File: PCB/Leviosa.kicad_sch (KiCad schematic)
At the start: 76 parts, among them J1 Barrel_Jack, J2 Conn_01x05_Socket, J3 2.54mm 1x03 Spare, Q1 NCE0110K, U1 SS495A, U2 LM321, U3 TPS1H200AQDGNRQ1, U4 INA199A3DCKR, U5 LM393, U6 L78L10_SOT89, U7 MX27517, U8 AZ1117CH2-3.3, U9 STM32G030F6Px

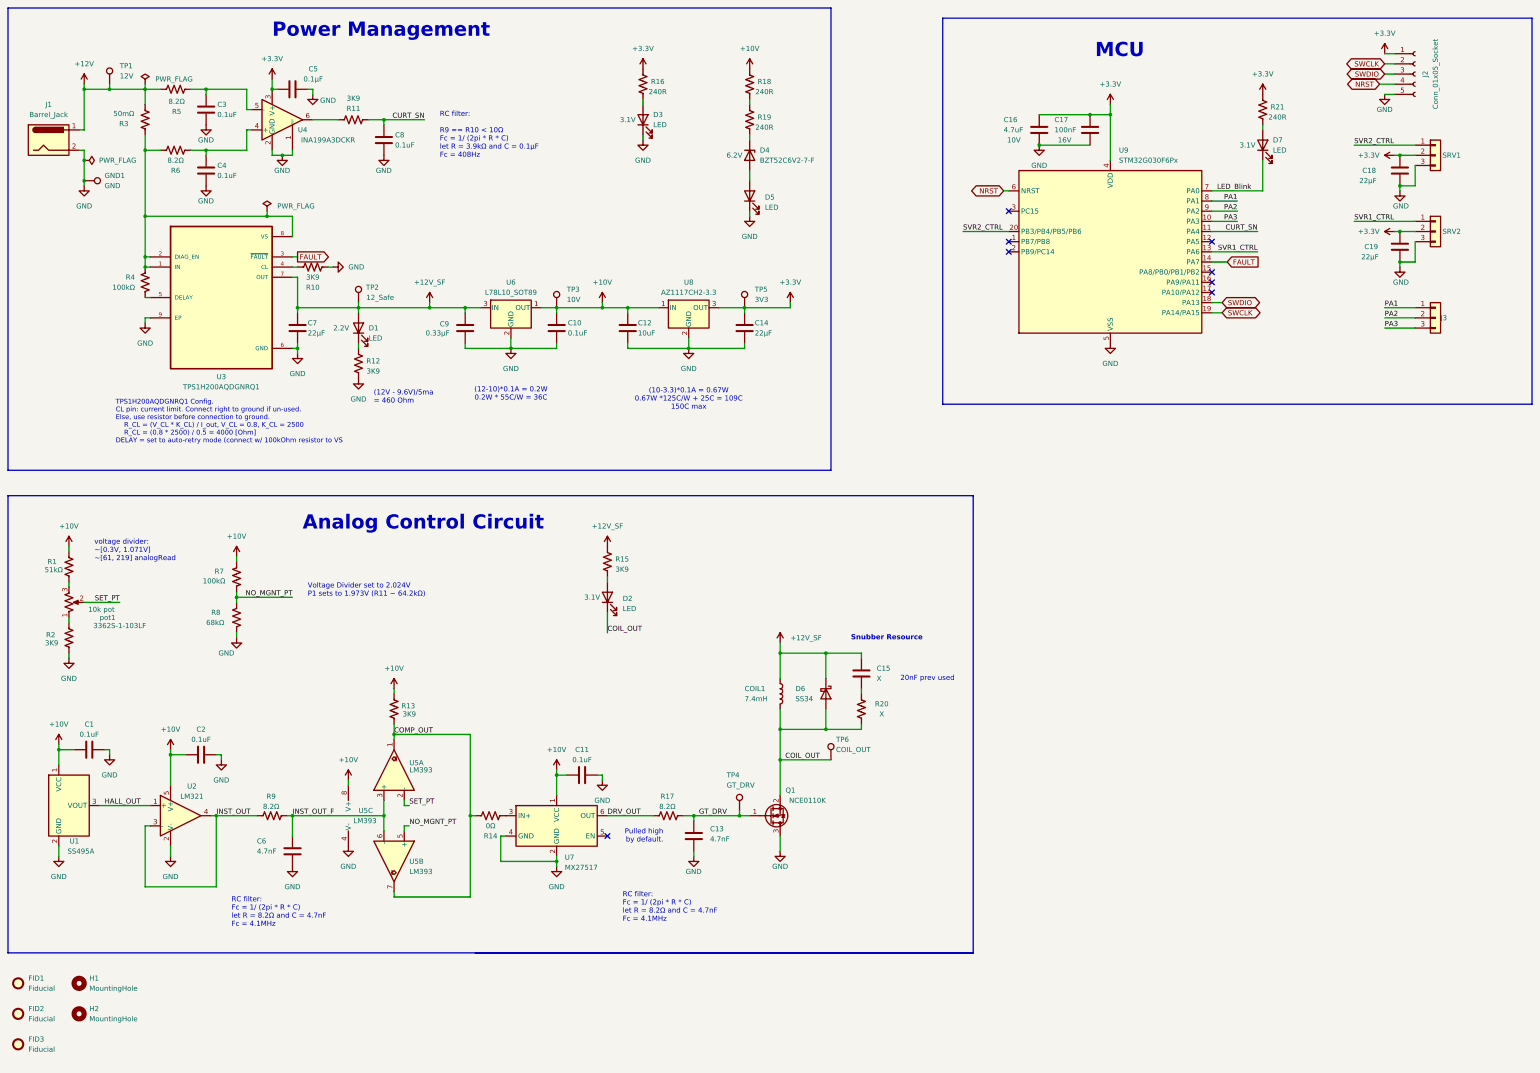
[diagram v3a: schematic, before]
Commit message: Snubber Add and Current sense reloc
Moved current sense circuit to just the coil

Added a snubber footprints to the mosfet, dont have to be used but footprints allow the possibility
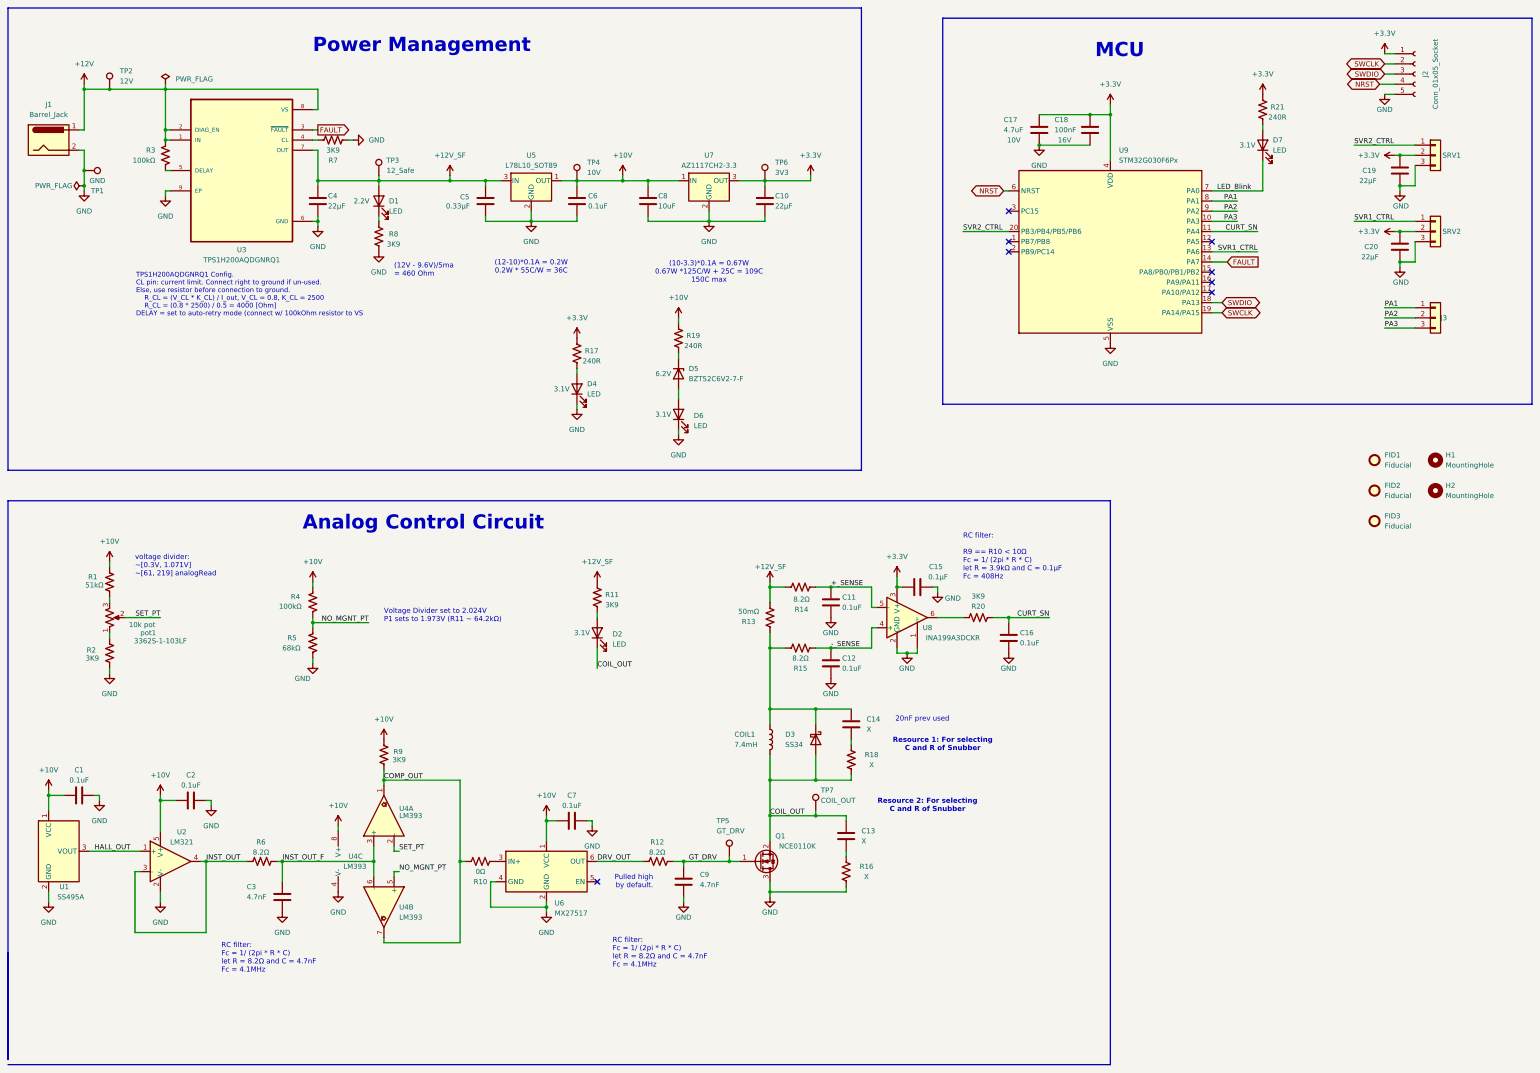
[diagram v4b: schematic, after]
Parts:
- removed R18: 240R, Resistor_SMD:R_0603_1608Metric, symbol Device:R_US
- added C13: X, Capacitor_SMD:C_0805_2012Metric_Pad1.18x1.45mm_HandSolder, symbol Device:C
- added R16: X, Resistor_SMD:R_0805_2012Metric_Pad1.20x1.40mm_HandSolder, symbol Device:R_US
- C11: renamed from C3; footprint Capacitor_SMD:C_1206_3216Metric -> Capacitor_SMD:C_0805_2012Metric
- C12: renamed from C4; footprint Capacitor_SMD:C_1206_3216Metric -> Capacitor_SMD:C_0805_2012Metric
- R14: renamed from R5; footprint Resistor_SMD:R_1206_3216Metric -> Resistor_SMD:R_0805_2012Metric
- R15: renamed from R6; footprint Resistor_SMD:R_1206_3216Metric -> Resistor_SMD:R_0805_2012Metric
- renumbered C14 to C10, C15 to C14, C5 to C15, C8 to C16, C16 to C17, C17 to C18, C18 to C19, C19 to C20, C6 to C3, C7 to C4, C9 to C5, C10 to C6, C11 to C7, C12 to C8, C13 to C9, D6 to D3, D3 to D4, D4 to D5, D5 to D6, R14 to R10, R15 to R11, R17 to R12, R3 to R13, R16 to R17, R20 to R18, R11 to R20, R4 to R3, R7 to R4, R8 to R5, R9 to R6, R10 to R7, R12 to R8, R13 to R9, GND1 to TP1, TP1 to TP2, TP2 to TP3, TP3 to TP4, TP4 to TP5, TP5 to TP6, TP6 to TP7, U5 to U4, U6 to U5, U7 to U6, U8 to U7, U4 to U8
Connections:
- net +10V: now also R19.1
- net +12V: now also R3.2, U3.1 (IN), U3.2 (DIAG_EN), U3.8 (VS); no longer R13.1, R14.1
- net +12V_SF: now also R13.1, R14.1; no longer C14.1, COIL1.1, D3.1 (K)
- net COIL_OUT: now also C13.1
- net GND: now also R16.1
- net +_SENSE: now reaches C11.2, R14.2, U8.5 (-)
- net -_SENSE: now reaches C12.2, R15.2, U8.4 (+)
- new net: C14.1, COIL1.1, D3.1 (K), R13.2, R15.1
- new net: C13.2, R16.2
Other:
- note added: "Resource 1: For selecting C and R of Snubber"
- note added: "Resource 2: For selecting C and R of Snubber"
- note removed: "Snubber Resource"
- moved on the sheet: C1, C10, C11, C12, C14, C15, C16, C2, C3, C4, C5, C6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
